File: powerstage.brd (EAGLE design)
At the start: 42 x 43.5 mm, 40 parts, among them CON1 PINHEAD_1X10-2-FEMALE, CON2 BATTERY_CON-2P-XT30-RA, CON3 PINHEAD_1X10-2-FEMALE, IC5 MCP9700, Q1 BUK7K6R2-40EX, Q2 BUK7K6R2-40EX, Q3 BUK7K6R2-40EX

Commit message: powerstage updates
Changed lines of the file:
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@@
 <setting verticaltext="up"/>
 </settings>
-<grid distance="0.05" unitdist="mm" unit="mm" style="lines" multiple="2" display="yes" altdistance="5" altunitdist="mil" altunit="mil"/>
+<grid distance="0.025" unitdist="mm" unit="mm" style="lines" multiple="2" display="yes" altdistance="5" altunitdist="mil" altunit="mil"/>
 <layers>
 <layer number="1" name="Top" color="4" fill="1" visible="yes" active="yes"/>
@@
 <layer number="25" name="tNames" color="7" fill="1" visible="yes" active="yes"/>
 <layer number="26" name="bNames" color="7" fill="1" visible="no" active="yes"/>
-<layer number="27" name="tValues" color="7" fill="1" visible="no" active="yes"/>
+<layer number="27" name="tValues" color="7" fill="1" visible="yes" active="yes"/>
 <layer number="28" name="bValues" color="7" fill="1" visible="no" active="yes"/>
 <layer number="29" name="tStop" color="7" fill="3" visible="no" active="yes"/>
@@
 <vertex x="6.3" y="10.35"/>
 </polygon>
-<polygon width="0.1524" layer="1" thermals="no" rank="3">
-<vertex x="6.3" y="15.15"/>
-<vertex x="-10.25" y="15.15"/>
+<polygon width="0.1524" layer="1" thermals="no" rank="4">
+<vertex x="6.3" y="15.175"/>
+<vertex x="-10.25" y="15.175"/>
 <vertex x="-10.25" y="10.35"/>
 <vertex x="6.3" y="10.35"/>
@@
 <contactref element="Q3" pad="5" route="any" routetag="T2.D"/>
 <contactref element="Q3" pad="1"/>
-<polygon width="0.1524" layer="1" thermals="no" rank="2">
+<polygon width="0.1524" layer="1" thermals="no" rank="3">
 <vertex x="0.2" y="9.8"/>
 <vertex x="0.2" y="15.8"/>
@@
 <contactref element="Q1" pad="1"/>
 <contactref element="B" pad="P$1"/>
-<polygon width="0.1524" layer="1" thermals="no">
+<polygon width="0.1524" layer="1" thermals="no" rank="2">
 <vertex x="-6.45" y="9.8"/>
 <vertex x="-6.45" y="19.4"/>

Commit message: DUCK is here
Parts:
- added U$2: (no value), logo:DUCK-8.5X7.5-MASK
- C1, C2, C3, C4, C5, C6: value (none) -> 68µF
- C31, C35, C58, C62, C63, C64: value 4.7µF -> 10µF; device myxa_masterlib:C1210 -> C_digikey:C1210
- Q1, Q2, Q3: value BUK7K6R2-40EX -> BUK9K6R2-40E,115
- R18, R5: value 1 mOhms -> 3 mOhms

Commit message: OSHW logo
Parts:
- added U$4: (no value), logo:OSHW-10.5X11.5
- moved U$1 4.60 mm to (5.20, 2.00)
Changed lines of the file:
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@@
 <drawing>
 <settings>
-<setting alwaysvectorfont="no"/>
+<setting alwaysvectorfont="yes"/>
 <setting verticaltext="up"/>
 </settings>
@@
 <layer number="14" name="Route14" color="22" fill="1" visible="no" active="no"/>
 <layer number="15" name="Route15" color="46" fill="6" visible="no" active="yes"/>
-<layer number="16" name="Bottom" color="1" fill="1" visible="yes" active="yes"/>
+<layer number="16" name="Bottom" color="1" fill="1" visible="no" active="yes"/>
 <layer number="17" name="Pads" color="2" fill="1" visible="yes" active="yes"/>
 <layer number="18" name="Vias" color="2" fill="1" visible="yes" active="yes"/>
@@
 <layer number="20" name="Dimension" color="24" fill="1" visible="yes" active="yes"/>
 <layer number="21" name="tPlace" color="7" fill="1" visible="yes" active="yes"/>
-<layer number="22" name="bPlace" color="7" fill="1" visible="yes" active="yes"/>
+<layer number="22" name="bPlace" color="7" fill="1" visible="no" active="yes"/>
 <layer number="23" name="tOrigins" color="15" fill="1" visible="yes" active="yes"/>
-<layer number="24" name="bOrigins" color="15" fill="1" visible="yes" active="yes"/>
+<layer number="24" name="bOrigins" color="15" fill="1" visible="no" active="yes"/>
 <layer number="25" name="tNames" color="7" fill="1" visible="yes" active="yes"/>
-<layer number="26" name="bNames" color="7" fill="1" visible="yes" active="yes"/>
+<layer number="26" name="bNames" color="7" fill="1" visible="no" active="yes"/>
 <layer number="27" name="tValues" color="7" fill="1" visible="yes" active="yes"/>
 <layer number="28" name="bValues" color="7" fill="1" visible="no" active="yes"/>
-<layer number="29" name="tStop" color="7" fill="3" visible="yes" active="yes"/>
+<layer number="29" name="tStop" color="7" fill="3" visible="no" active="yes"/>
 <layer number="30" name="bStop" color="7" fill="6" visible="no" active="yes"/>
 <layer number="31" name="tCream" color="7" fill="4" visible="no" active="yes"/>
@@
 <layer number="48" name="Document" color="7" fill="1" visible="no" active="yes"/>
 <layer number="49" name="Reference" color="7" fill="1" visible="no" active="yes"/>
-<layer number="50" name="dxf" color="7" fill="1" visible="no" active="no"/>
+<layer number="50" name="dxf" color="7" fill="1" visible="yes" active="yes"/>
 <layer number="51" name="tDocu" color="7" fill="1" visible="yes" active="yes"/>
-<layer number="52" name="bDocu" color="7" fill="1" visible="yes" active="yes"/>
+<layer number="52" name="bDocu" color="7" fill="1" visible="no" active="yes"/>
 <layer number="53" name="tGND_GNDA" color="7" fill="9" visible="no" active="no"/>
 <layer number="54" name="bGND_GNDA" color="1" fill="9" visible="no" active="no"/>
@@
 </layers>
 <board>
-<fusionsync huburn="a.cGVyc29uYWw6dWUyYWE4ZDY4" projecturn="a.cGVyc29uYWw6dWUyYWE4ZDY4IzIwMTgxMTA4MTU5MTUwNTA2" f3durn="urn:adsk.wipprod:dm.lineage:VvqHLlV8QrG5oXj_COKgWw" pcbguid="ff29db28-3bc8-4e0e-90a2-548e6287645e" lastpulledtime="" lastsyncedchangeguid="8f113dfe-18f2-01bf-0aa9-46ebdb4811d6"/>
+<fusionsync huburn="a.cGVyc29uYWw6dWUyYWE4ZDY4" projecturn="a.cGVyc29uYWw6dWUyYWE4ZDY4IzIwMTgxMTA4MTU5MTUwNTA2" f3durn="urn:adsk.wipprod:dm.lineage:VvqHLlV8QrG5oXj_COKgWw" pcbguid="ff29db28-3bc8-4e0e-90a2-548e6287645e" lastpulledtime="" lastsyncedchangeguid="5e2d1aac-41dd-a679-520f-711cd63c8ed2"/>
 <plain>
 <wire x1="0" y1="0" x2="0" y2="21" width="0.1524" layer="49" style="shortdash" locked="yes"/>
@@
 </element>
 <element name="U$13" library="pixhawk_esc_1.5_master_lib" package="ZUBAX_LOGO_5X10" value="" x="-6.225" y="-5.475" smashed="yes"/>
-<element name="U$1" library="pixhawk_esc_1.5_master_lib" package="ZUBAX_LOGO_5X10" value="" x="5.2" y="-2.6" smashed="yes" rot="MR0"/>
+<element name="U$1" library="pixhawk_esc_1.5_master_lib" package="ZUBAX_LOGO_5X10" value="" x="5.2" y="2" smashed="yes" rot="MR0"/>
 <element name="U$2" library="logo" library_urn="urn:adsk.eagle:library:6668987" package="DUCK-8.5X7.5-MASK" value="" x="-4.5" y="-22.475" smashed="yes"/>
+<element name="U$4" library="logo" library_urn="urn:adsk.eagle:library:6668987" package="OSHW-10.5X11.5" value="" x="5.475" y="-8.525" smashed="yes" rot="MR0"/>
 </elements>
 <signals>

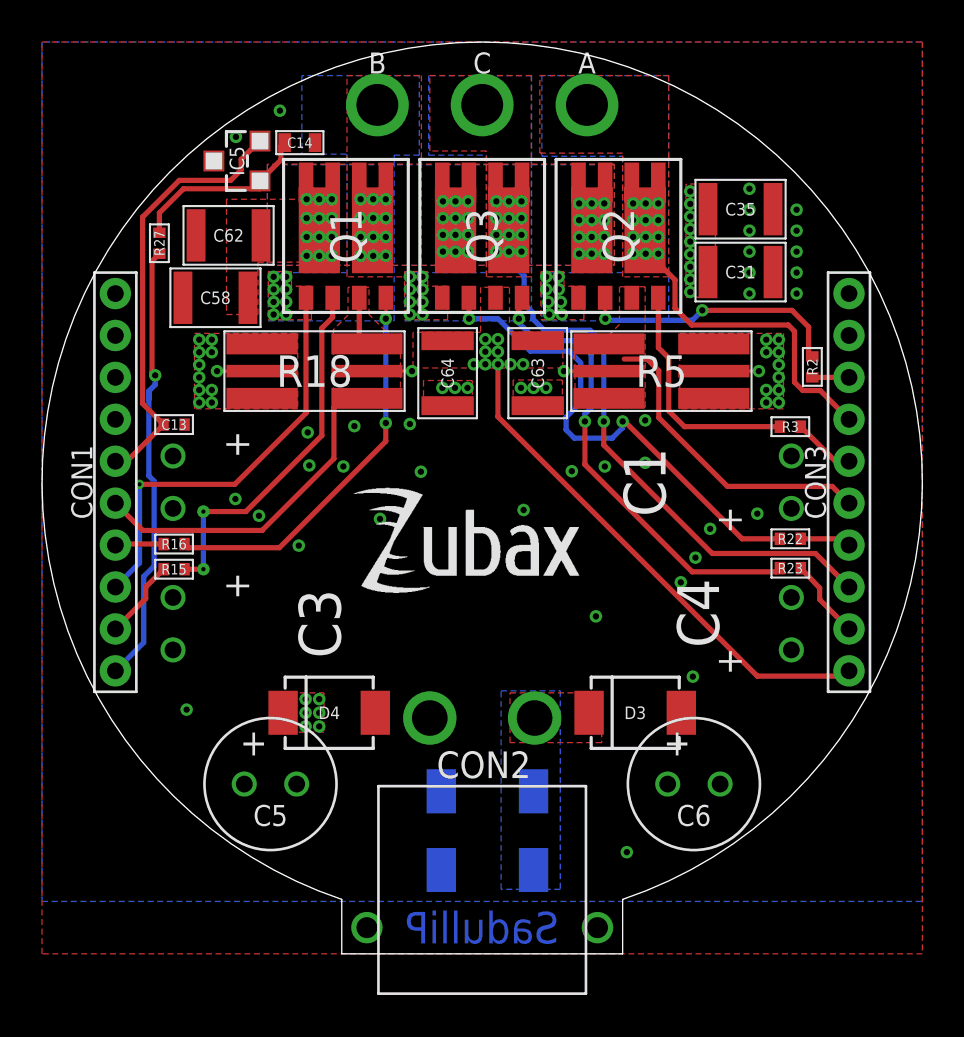
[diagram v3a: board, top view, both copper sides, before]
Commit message: Routing is complete again. Now with BEC output
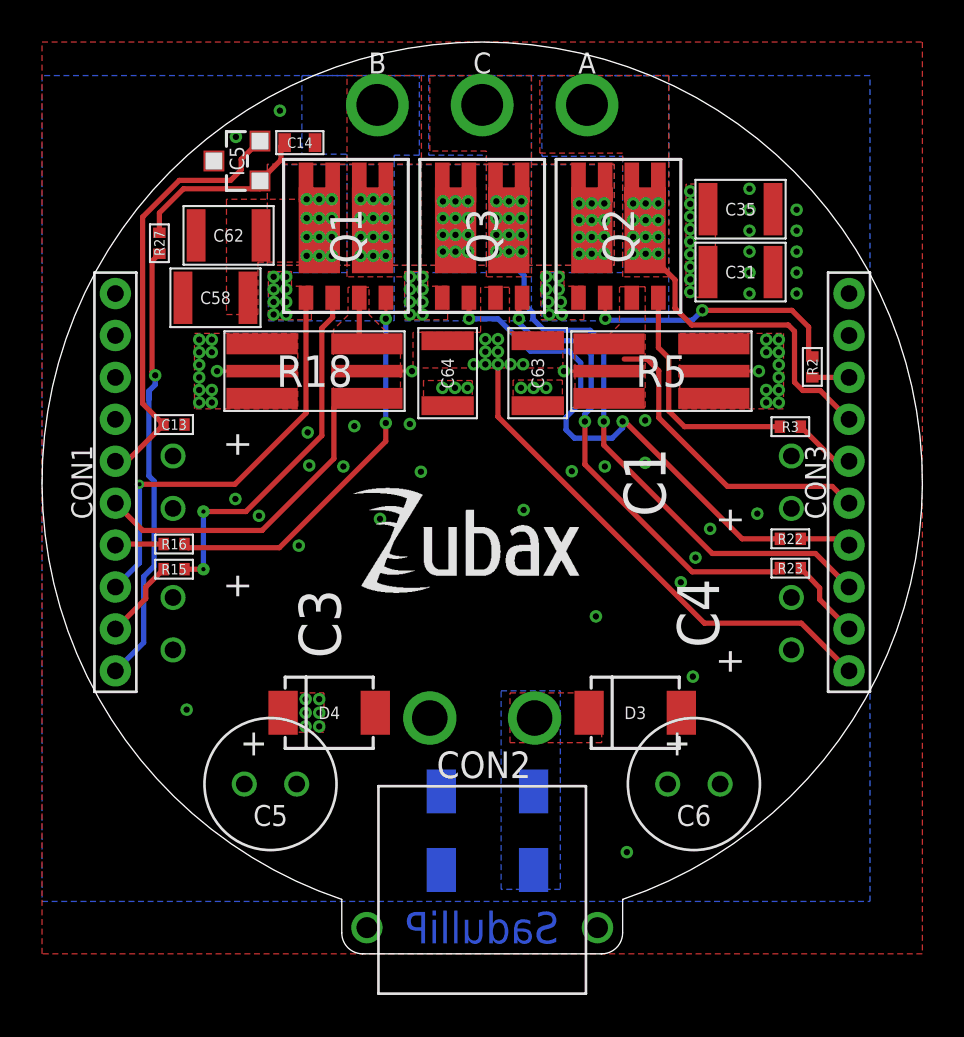
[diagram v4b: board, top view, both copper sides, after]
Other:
- outline, holes or cut-outs redrawn
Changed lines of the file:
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@@
 <drawing>
 <settings>
-<setting alwaysvectorfont="yes"/>
+<setting alwaysvectorfont="no"/>
 <setting verticaltext="up"/>
 </settings>
@@
 </layers>
 <board>
-<fusionsync huburn="a.cGVyc29uYWw6dWUyYWE4ZDY4" projecturn="a.cGVyc29uYWw6dWUyYWE4ZDY4IzIwMTgxMTA4MTU5MTUwNTA2" f3durn="urn:adsk.wipprod:dm.lineage:VvqHLlV8QrG5oXj_COKgWw" pcbguid="ff29db28-3bc8-4e0e-90a2-548e6287645e" lastpulledtime="" lastsyncedchangeguid="5e2d1aac-41dd-a679-520f-711cd63c8ed2"/>
 <plain>
 <wire x1="0" y1="0" x2="0" y2="21" width="0.1524" layer="49" style="shortdash" locked="yes"/>
@@
 <wire x1="20" y1="-20" x2="-20" y2="-20" width="0.01" layer="48" locked="yes"/>
 <wire x1="-20" y1="-20" x2="-20" y2="0" width="0.01" layer="48" locked="yes"/>
-<wire x1="6.7" y1="-22.5" x2="6.7" y2="-19.9025" width="0.01" layer="20"/>
+<wire x1="-6.7" y1="-19.9025" x2="-6.7" y2="-21.5" width="0.01" layer="20"/>
+<wire x1="-6.7" y1="-21.5" x2="-5.7" y2="-22.5" width="0.01" layer="20" curve="90"/>
+<wire x1="-5.7" y1="-22.5" x2="5.7" y2="-22.5" width="0.01" layer="20"/>
+<wire x1="5.7" y1="-22.5" x2="6.7" y2="-21.5" width="0.01" layer="20" curve="90"/>
+<wire x1="6.7" y1="-21.5" x2="6.7" y2="-19.9025" width="0.01" layer="20"/>
 <wire x1="6.7" y1="-19.9025" x2="-6.7" y2="-19.9025" width="0.01" layer="20" curve="322.789323"/>
-<wire x1="-6.7" y1="-19.9025" x2="-6.7" y2="-22.5" width="0.01" layer="20"/>
-<wire x1="-6.7" y1="-22.5" x2="6.7" y2="-22.5" width="0.01" layer="20"/>
 <wire x1="-0.725" y1="9.45" x2="1.375" y2="9.45" width="0.15" layer="41"/>
 <wire x1="1.375" y1="7.5" x2="1.375" y2="9.45" width="0.15" layer="41"/>
@@
 <wire x1="11.7" y1="-0.2" x2="16.7" y2="-0.2" width="0.25" layer="1"/>
 <wire x1="8.425" y1="3.075" x2="11.7" y2="-0.2" width="0.25" layer="1"/>
-<wire x1="6.05" y1="4" x2="6.775" y2="5.875" width="0" layer="19" extent="1-1"/>
+<wire x1="6.775" y1="5.875" x2="6.05" y2="4" width="0" layer="19" extent="1-1"/>
 </signal>
 <signal name="PHASE_A" class="1">
@@
 <contactref element="S1" pad="IN"/>
 <contactref element="CON3" pad="1"/>
-<wire x1="17.5" y1="-9" x2="17.25" y2="-9.25" width="0.25" layer="1"/>
-<wire x1="13.125" y1="-9.25" x2="0.75" y2="3.125" width="0.25" layer="1"/>
-<wire x1="17.25" y1="-9.25" x2="13.125" y2="-9.25" width="0.25" layer="1"/>
+<wire x1="10.6" y1="-6.725" x2="0.75" y2="3.125" width="0.25" layer="1"/>
+<wire x1="17.5" y1="-9" x2="15.225" y2="-6.725" width="0.25" layer="1"/>
+<wire x1="15.225" y1="-6.725" x2="10.6" y2="-6.725" width="0.25" layer="1"/>
 <wire x1="0.75" y1="3.125" x2="0.75" y2="5.625" width="0.25" layer="1"/>
 </signal>
@@
 <contactref element="CON2" pad="-"/>
 <polygon width="0.1524" layer="16" rank="5">
-<vertex x="0" y="21"/>
-<vertex x="-21" y="21"/>
+<vertex x="0" y="19.4"/>
+<vertex x="-21" y="19.4"/>
 <vertex x="-21" y="-20"/>
-<vertex x="21" y="-20"/>
-<vertex x="21" y="21"/>
+<vertex x="18.5" y="-20"/>
+<vertex x="18.5" y="19.4"/>
 </polygon>
 <via x="13.55" y="6.8" extent="1-16" drill="0.3" diameter="0.6"/>
@@
 </polygon>
 <polygon width="0.3" layer="15" rank="5">
-<vertex x="-21" y="21"/>
-<vertex x="-21" y="-20"/>
-<vertex x="21" y="-20"/>
-<vertex x="21" y="21"/>
+<vertex x="-18.5" y="19.4"/>
+<vertex x="-18.5" y="-20"/>
+<vertex x="18.5" y="-20"/>
+<vertex x="18.5" y="19.4"/>
 </polygon>
 <contactref element="IC5" pad="3"/>
@@
 </note>
 <note version="8.3" severity="warning">
-Since Version 8.3, EAGLE supports Fusion synchronisation.
-This feature will not be available in this version and saving
-the document will break the link to the Fusion PCB feature.
-</note>
-<note version="8.3" severity="warning">
